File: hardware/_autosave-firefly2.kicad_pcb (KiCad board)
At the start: 2 copper layers, 41.4 x 41.3 mm, 19 parts, among them J1 Conn_01x01, J2 614105150721, J3 CONN_01X01, P2 CONN_01X03, P3 CONN_01X04, P4 CONN_01X05, P5 CONN_01X01, U1 SAMD21E18, U2 RFM69CW, U3 MIC5504

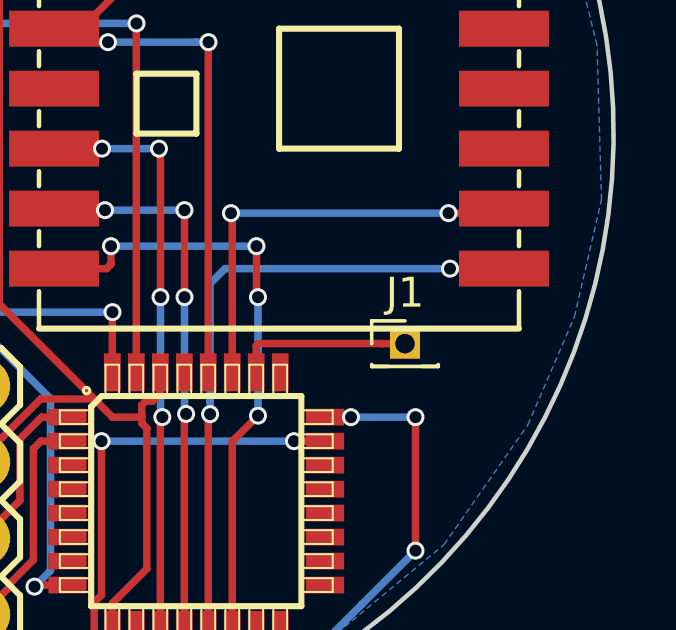
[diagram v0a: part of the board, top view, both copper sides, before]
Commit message: Board rev 2.3
- Fix orientation for UC (in homebrew)
- Fix 3v3 -> 5v on programming header silk
- Flipped headers so the bottom has actual pads
- Exposed the reset pin
- Fixed LED signal shorted to ground pour

Change-Id: I21f070da93fd6e851c38ed11e53aa0c7e677237e
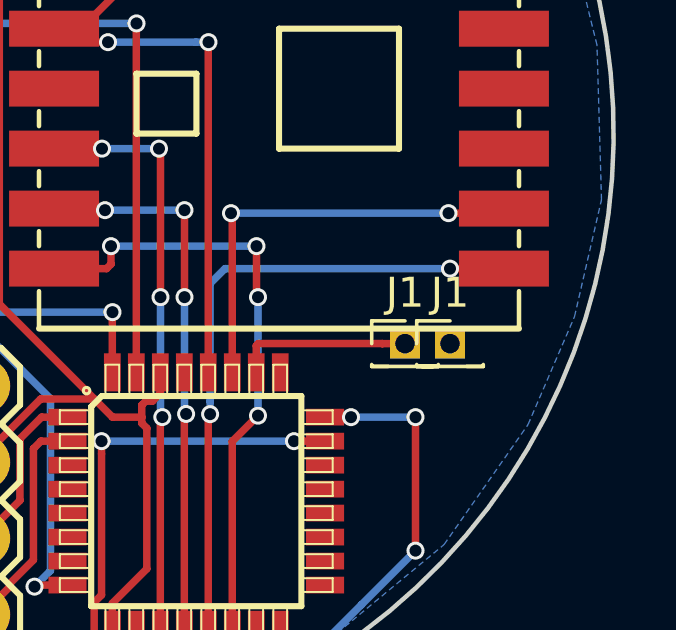
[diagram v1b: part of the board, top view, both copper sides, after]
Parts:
- added J1: Conn_01x01, Pin_Headers:Pin_Header_Straight_1x01_Pitch1.27mm, F.Cu at (175.2, 70.5)
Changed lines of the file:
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@@
 (kicad_pcb (version 4) (host pcbnew 4.0.7+dfsg1-1ubuntu2)
   (general
-    (links 50)
-    (no_connects 1)
-    (area 139.25939 42.824999 180.78061 84.26061)
+    (links 51)
+    (no_connects 0)
+    (area 139.25939 42.824999 187.034459 84.714286)
     (thickness 1.6)
     (drawings 141)
     (tracks 292)
     (zones 0)
-    (modules 19)
+    (modules 20)
     (nets 44)
   )
@@
     (35 F.Paste user hide)
     (36 B.SilkS user hide)
-    (37 F.SilkS user hide)
+    (37 F.SilkS user)
     (38 B.Mask user hide)
     (39 F.Mask user hide)
@@
     (mod_text_size 1 1)
     (mod_text_width 0.15)
-    (pad_size 1.7 1.7)
-    (pad_drill 1)
+    (pad_size 1 1)
+    (pad_drill 0.65)
     (pad_to_mask_clearance 0.2)
     (aux_axis_origin 139.4 84.6)
     (visible_elements FFFFFF7F)
     (pcbplotparams
-      (layerselection 0x310fc_80000001)
+      (layerselection 0x330fc_80000001)
       (usegerberextensions false)
       (excludeedgelayer true)
@@
     (add_net USB_D-)
   )
+  (module Pin_Headers:Pin_Header_Straight_1x01_Pitch1.27mm (layer F.Cu)
+    (at 175.25 70.5)
+    (descr "Through hole straight pin header, 1x01, 1.27mm pitch, single row")
+    (tags "Through hole pin header THT 1x01 1.27mm single row")
+    (fp_text reference J1 (at 0 -1.695) (layer F.SilkS)
+      (effects (font (size 1 1) (thickness 0.15)))
+    )
+    (fp_text value Conn_01x01 (at 0 1.695) (layer F.Fab)
+      (effects (font (size 1 1) (thickness 0.15)))
+    )
+    (fp_line (start -0.525 -0.635) (end 1.05 -0.635) (layer F.Fab) (width 0.1))
+    (fp_line (start 1.05 -0.635) (end 1.05 0.635) (layer F.Fab) (width 0.1))
+    (fp_line (start 1.05 0.635) (end -1.05 0.635) (layer F.Fab) (width 0.1))
+    (fp_line (start -1.05 0.635) (end -1.05 -0.11) (layer F.Fab) (width 0.1))
+    (fp_line (start -1.05 -0.11) (end -0.525 -0.635) (layer F.Fab) (width 0.1))
+    (fp_line (start -1.11 0.76) (end 1.11 0.76) (layer F.SilkS) (width 0.12))
+    (fp_line (start -1.11 0.76) (end -1.11 0.695) (layer F.SilkS) (width 0.12))
+    (fp_line (start 1.11 0.76) (end 1.11 0.695) (layer F.SilkS) (width 0.12))
+    (fp_line (start -1.11 0.76) (end -0.563471 0.76) (layer F.SilkS) (width 0.12))
+    (fp_line (start 0.563471 0.76) (end 1.11 0.76) (layer F.SilkS) (width 0.12))
+    (fp_line (start -1.11 0) (end -1.11 -0.76) (layer F.SilkS) (width 0.12))
+    (fp_line (start -1.11 -0.76) (end 0 -0.76) (layer F.SilkS) (width 0.12))
+    (fp_line (start -1.55 -1.15) (end -1.55 1.15) (layer F.CrtYd) (width 0.05))
+    (fp_line (start -1.55 1.15) (end 1.55 1.15) (layer F.CrtYd) (width 0.05))
+    (fp_line (start 1.55 1.15) (end 1.55 -1.15) (layer F.CrtYd) (width 0.05))
+    (fp_line (start 1.55 -1.15) (end -1.55 -1.15) (layer F.CrtYd) (width 0.05))
+    (fp_text user %R (at 0 0 90) (layer F.Fab)
+      (effects (font (size 1 1) (thickness 0.15)))
+    )
+    (pad 1 thru_hole rect (at 0 0) (size 1 1) (drill 0.65) (layers *.Cu *.Mask)
+      (net 1 GND))
+    (model ${KISYS3DMOD}/Pin_Headers.3dshapes/Pin_Header_Straight_1x01_Pitch1.27mm.wrl
+      (at (xyz 0 0 0))
+      (scale (xyz 1 1 1))
+      (rotate (xyz 0 0 0))
+    )
+  )
   (module SparkFun-Connectors:1X03 placed (layer F.Cu)
